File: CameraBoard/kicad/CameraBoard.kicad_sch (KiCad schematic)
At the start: 58 parts, among them IC1 MP2659GQ-0000-Z, Q1 SUD08P06-155L, Q2 SUD08P06-155L, Q3 SUD08P06-155L, U1 LM2678SD-12/NOPB

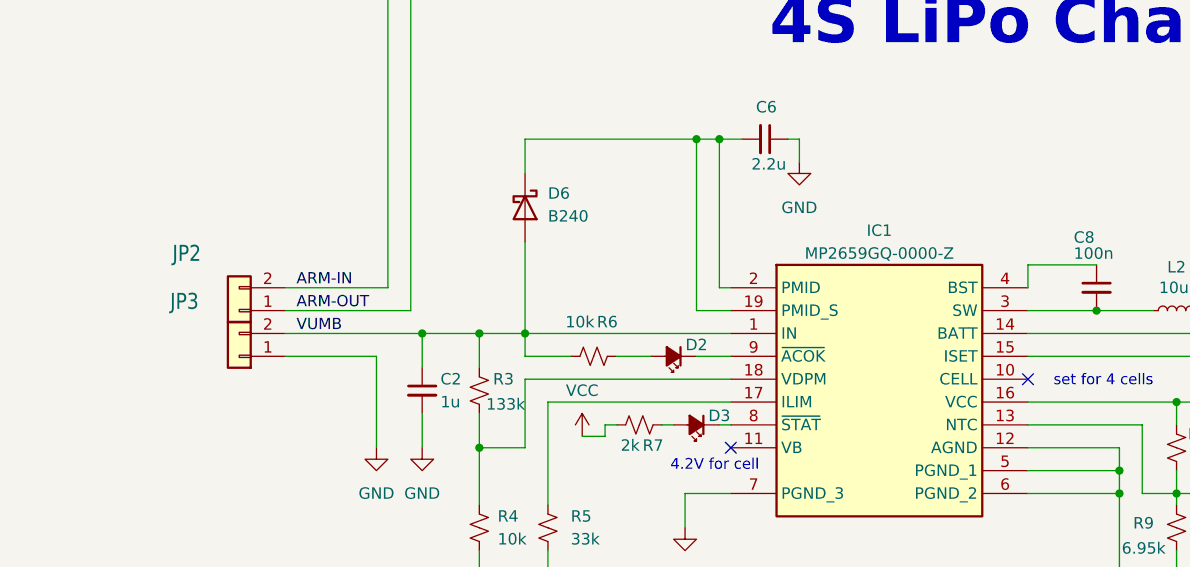
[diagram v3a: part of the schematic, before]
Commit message: PCB made from new schematic
Made the PCB. There are a few weird errors.
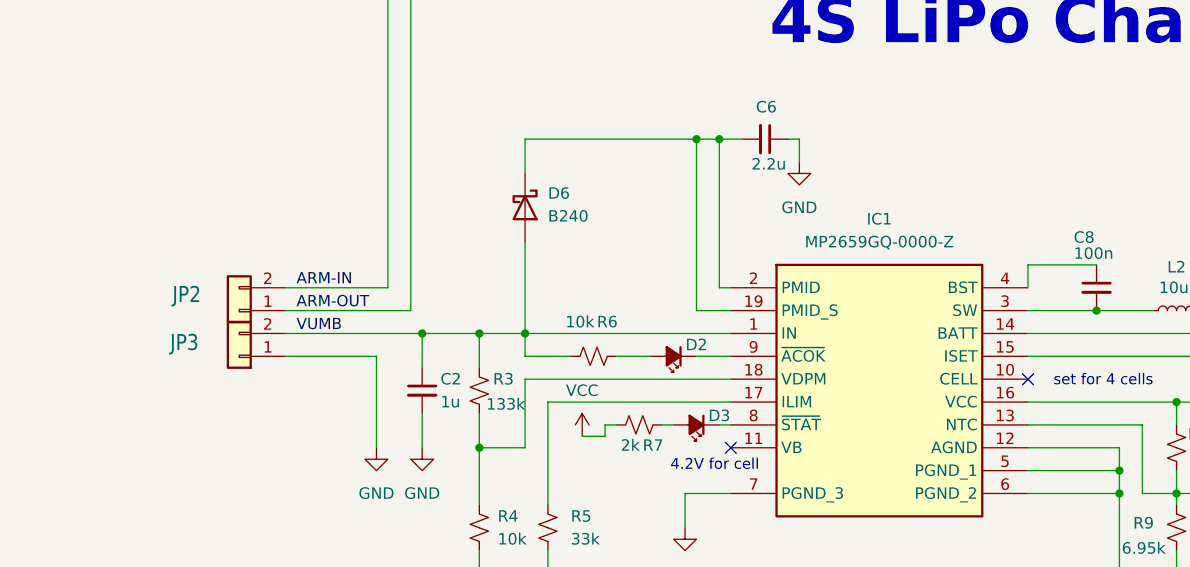
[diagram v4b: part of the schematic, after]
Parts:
- D2, D3, D5: footprint CameraBoard:CHIPLED_0603_259 -> LED_SMD:LED_0603_1608Metric
- IC1: footprint MP2659GQ0000Z -> psas-footprints:MP2659GQ0000Z; symbol MP2659GQ-0000-Z:MP2659GQ-0000-Z -> psas-libraries:MP2659GQ-0000-Z
- JP1, JP2, JP3: footprint Connector_PinHeader_2.54mm:PinHeader_1x02_P2.54mm_Vertical_SMD_Pin1Left -> Connector_PinHeader_2.54mm:PinHeader_1x02_P2.54mm_Vertical
- JP10, JP11, JP12, JP13, JP14, JP5, JP6, JP7, JP8, JP9: footprint Connector_PinHeader_2.54mm:PinHeader_1x03_P2.54mm_Vertical_SMD_Pin1Left -> Connector_PinHeader_2.54mm:PinHeader_1x03_P2.54mm_Vertical
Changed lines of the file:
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@@
 			)
 		)
-		(property "Footprint" "Connector_PinHeader_2.54mm:PinHeader_1x03_P2.54mm_Vertical_SMD_Pin1Left"
+		(property "Footprint" "Connector_PinHeader_2.54mm:PinHeader_1x03_P2.54mm_Vertical"
 			(at 271.78 238.76 0)
 			(hide yes)
@@
 			)
 		)
-		(property "Footprint" "CameraBoard:CHIPLED_0603_259"
+		(property "Footprint" "LED_SMD:LED_0603_1608Metric"
 			(at 205.74 236.22 90)
 			(hide yes)
@@
 			)
 		)
-		(property "Footprint" "Connector_PinHeader_2.54mm:PinHeader_1x03_P2.54mm_Vertical_SMD_Pin1Left"
+		(property "Footprint" "Connector_PinHeader_2.54mm:PinHeader_1x03_P2.54mm_Vertical"
 			(at 351.79 160.02 0)
 			(hide yes)
@@
 			)
 		)
-		(property "Footprint" "CameraBoard:CHIPLED_0603_259"
+		(property "Footprint" "LED_SMD:LED_0603_1608Metric"
 			(at 113.03 114.3 90)
 			(hide yes)
@@
 			)
 		)
-		(property "Footprint" "Connector_PinHeader_2.54mm:PinHeader_1x02_P2.54mm_Vertical_SMD_Pin1Left"
+		(property "Footprint" "Connector_PinHeader_2.54mm:PinHeader_1x02_P2.54mm_Vertical"
 			(at 33.02 176.53 0)
 			(hide yes)
@@
 			)
 		)
-		(property "Footprint" "Connector_PinHeader_2.54mm:PinHeader_1x03_P2.54mm_Vertical_SMD_Pin1Left"
+		(property "Footprint" "Connector_PinHeader_2.54mm:PinHeader_1x03_P2.54mm_Vertical"
 			(at 271.78 165.1 0)
 			(hide yes)
@@
 	)
 	(symbol
-		(lib_id "MP2659GQ-0000-Z:MP2659GQ-0000-Z")
-		(at 116.84 99.06 0)
+		(lib_id "psas-libraries:MP2659GQ-0000-Z")
+		(at 109.22 95.25 0)
 		(unit 1)
 		(body_style 1)
@@
 		(fields_autoplaced yes)
 		(property "Reference" "IC1"
-			(at 133.35 92.71 0)
+			(at 133.35 91.44 0)
 			(show_name no)
 			(do_not_autoplace no)
@@
 		)
 		(property "Value" "MP2659GQ-0000-Z"
-			(at 133.35 95.25 0)
+			(at 133.35 93.98 0)
 			(show_name no)
 			(do_not_autoplace no)
@@
 			)
 		)
-		(property "Footprint" "MP2659GQ0000Z"
-			(at 146.05 193.98 0)
+		(property "Footprint" "psas-footprints:MP2659GQ0000Z"
+			(at 138.43 190.17 0)
 			(hide yes)
 			(show_name no)
@@
 		)
 		(property "Datasheet" "https://www.monolithicpower.com/en/documentview/productdocument/index/version/2/document_type/Datasheet/lang/en/sku/MP2659/"
-			(at 146.05 293.98 0)
+			(at 138.43 290.17 0)
 			(hide yes)
 			(show_name no)
@@
 		)
 		(property "Description" "Battery Management 36V 3A Switching Charger with Integrated MOSFETs and Input Power Management for 3-6 Cell Batteries"
-			(at 116.84 99.06 0)
+			(at 109.22 95.25 0)
 			(hide yes)
 			(show_name no)
@@
 		)
 		(property "Height" "1"
-			(at 146.05 493.98 0)
+			(at 138.43 490.17 0)
 			(hide yes)
 			(show_name no)
@@
 		)
 		(property "Manufacturer_Name" "Monolithic Power Systems (MPS)"
-			(at 146.05 593.98 0)
+			(at 138.43 590.17 0)
 			(hide yes)
 			(show_name no)
@@
 		)
 		(property "Manufacturer_Part_Number" "MP2659GQ-0000-Z"
-			(at 146.05 693.98 0)
+			(at 138.43 690.17 0)
 			(hide yes)
 			(show_name no)
@@
 		)
 		(property "Mouser Part Number" "946-MP2659GQ-0000-Z"
-			(at 146.05 793.98 0)
+			(at 138.43 790.17 0)
 			(hide yes)
 			(show_name no)
@@
 		)
 		(property "Mouser Price/Stock" "https://www.mouser.co.uk/ProductDetail/Monolithic-Power-Systems-MPS/MP2659GQ-0000-Z?qs=yqaQSyyJnNj9lFhPiaIeCQ%3D%3D"
-			(at 146.05 893.98 0)
+			(at 138.43 890.17 0)
 			(hide yes)
 			(show_name no)
@@
 		)
 		(property "Arrow Part Number" ""
-			(at 146.05 993.98 0)
+			(at 138.43 990.17 0)
 			(hide yes)
 			(show_name no)
@@
 		)
 		(property "Arrow Price/Stock" ""
-			(at 146.05 1093.98 0)
+			(at 138.43 1090.17 0)
 			(hide yes)
 			(show_name no)
@@
 		)
 		(property "DIS" ""
-			(at 116.84 99.06 0)
+			(at 109.22 95.25 0)
 			(hide yes)
 			(show_name no)
@@
 		)
 		(property "DPN" ""
-			(at 116.84 99.06 0)
+			(at 109.22 95.25 0)
 			(hide yes)
 			(show_name no)
@@
 		)
 		(property "MAN" ""
-			(at 116.84 99.06 0)
+			(at 109.22 95.25 0)
 			(hide yes)
 			(show_name no)
@@
 		)
 		(property "MPN" ""
-			(at 116.84 99.06 0)
+			(at 109.22 95.25 0)
 			(hide yes)
 			(show_name no)
@@
 		)
 		(property "Sim.Device" ""
-			(at 116.84 99.06 0)
+			(at 109.22 95.25 0)
 			(hide yes)
 			(show_name no)
@@
 			)
 		)
-		(property "Footprint" "Connector_PinHeader_2.54mm:PinHeader_1x03_P2.54mm_Vertical_SMD_Pin1Left"
+		(property "Footprint" "Connector_PinHeader_2.54mm:PinHeader_1x03_P2.54mm_Vertical"
 			(at 271.78 177.8 0)
 			(hide yes)
@@
 			)
 		)
-		(property "Footprint" "Connector_PinHeader_2.54mm:PinHeader_1x03_P2.54mm_Vertical_SMD_Pin1Left"
+		(property "Footprint" "Connector_PinHeader_2.54mm:PinHeader_1x03_P2.54mm_Vertical"
 			(at 271.78 228.6 0)
 			(hide yes)
@@
 			)
 		)
-		(property "Footprint" "Connector_PinHeader_2.54mm:PinHeader_1x03_P2.54mm_Vertical_SMD_Pin1Left"
+		(property "Footprint" "Connector_PinHeader_2.54mm:PinHeader_1x03_P2.54mm_Vertical"
 			(at 271.78 218.44 0)
 			(hide yes)
@@
 			)
 		)
-		(property "Footprint" "Connector_PinHeader_2.54mm:PinHeader_1x03_P2.54mm_Vertical_SMD_Pin1Left"
+		(property "Footprint" "Connector_PinHeader_2.54mm:PinHeader_1x03_P2.54mm_Vertical"
 			(at 271.78 187.96 0)
 			(hide yes)
@@
 			)
 		)
-		(property "Footprint" "CameraBoard:CHIPLED_0603_259"
+		(property "Footprint" "LED_SMD:LED_0603_1608Metric"
 			(at 110.49 106.68 90)
 			(hide yes)
@@
 			)
 		)
-		(property "Footprint" "Connector_PinHeader_2.54mm:PinHeader_1x03_P2.54mm_Vertical_SMD_Pin1Left"
+		(property "Footprint" "Connector_PinHeader_2.54mm:PinHeader_1x03_P2.54mm_Vertical"
 			(at 271.78 208.28 0)
 			(hide yes)
@@
 			)
 		)
-		(property "Footprint" "Connector_PinHeader_2.54mm:PinHeader_1x03_P2.54mm_Vertical_SMD_Pin1Left"
+		(property "Footprint" "Connector_PinHeader_2.54mm:PinHeader_1x03_P2.54mm_Vertical"
 			(at 271.78 152.4 0)
 			(hide yes)
@@
 			)
 		)
-		(property "Footprint" "Connector_PinHeader_2.54mm:PinHeader_1x03_P2.54mm_Vertical_SMD_Pin1Left"
+		(property "Footprint" "Connector_PinHeader_2.54mm:PinHeader_1x03_P2.54mm_Vertical"
 			(at 271.78 198.12 0)
 			(hide yes)
@@
 		(dnp no)
 		(property "Reference" "JP2"
-			(at 56.388 95.25 0)
+			(at 56.388 99.822 0)
 			(show_name no)
 			(do_not_autoplace no)
@@
 			)
 		)
-		(property "Footprint" "Connector_PinHeader_2.54mm:PinHeader_1x02_P2.54mm_Vertical_SMD_Pin1Left"
+		(property "Footprint" "Connector_PinHeader_2.54mm:PinHeader_1x02_P2.54mm_Vertical"
 			(at 62.23 101.6 0)
 			(hide yes)
@@
 		(dnp no)
 		(property "Reference" "JP3"
-			(at 56.134 100.584 0)
+			(at 56.134 105.156 0)
 			(show_name no)
 			(do_not_autoplace no)
@@
 			)
 		)
-		(property "Footprint" "Connector_PinHeader_2.54mm:PinHeader_1x02_P2.54mm_Vertical_SMD_Pin1Left"
+		(property "Footprint" "Connector_PinHeader_2.54mm:PinHeader_1x02_P2.54mm_Vertical"
 			(at 62.23 106.68 0)
 			(hide yes)

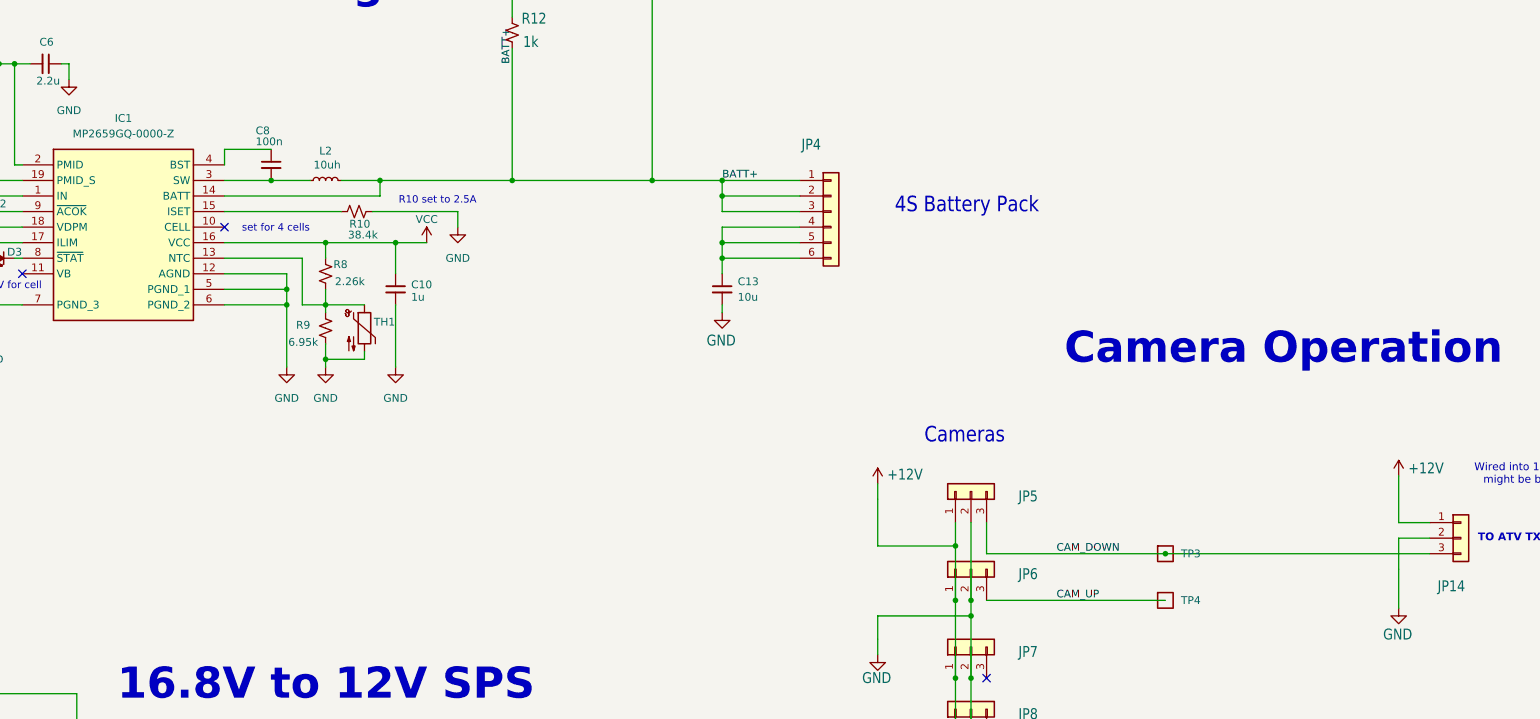
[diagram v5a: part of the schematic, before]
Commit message: Small updates to PCB
-Made text the same size
-Changed U1 symbol
-Added zones
-Moved connectors to more convenient location
-Moved leds together
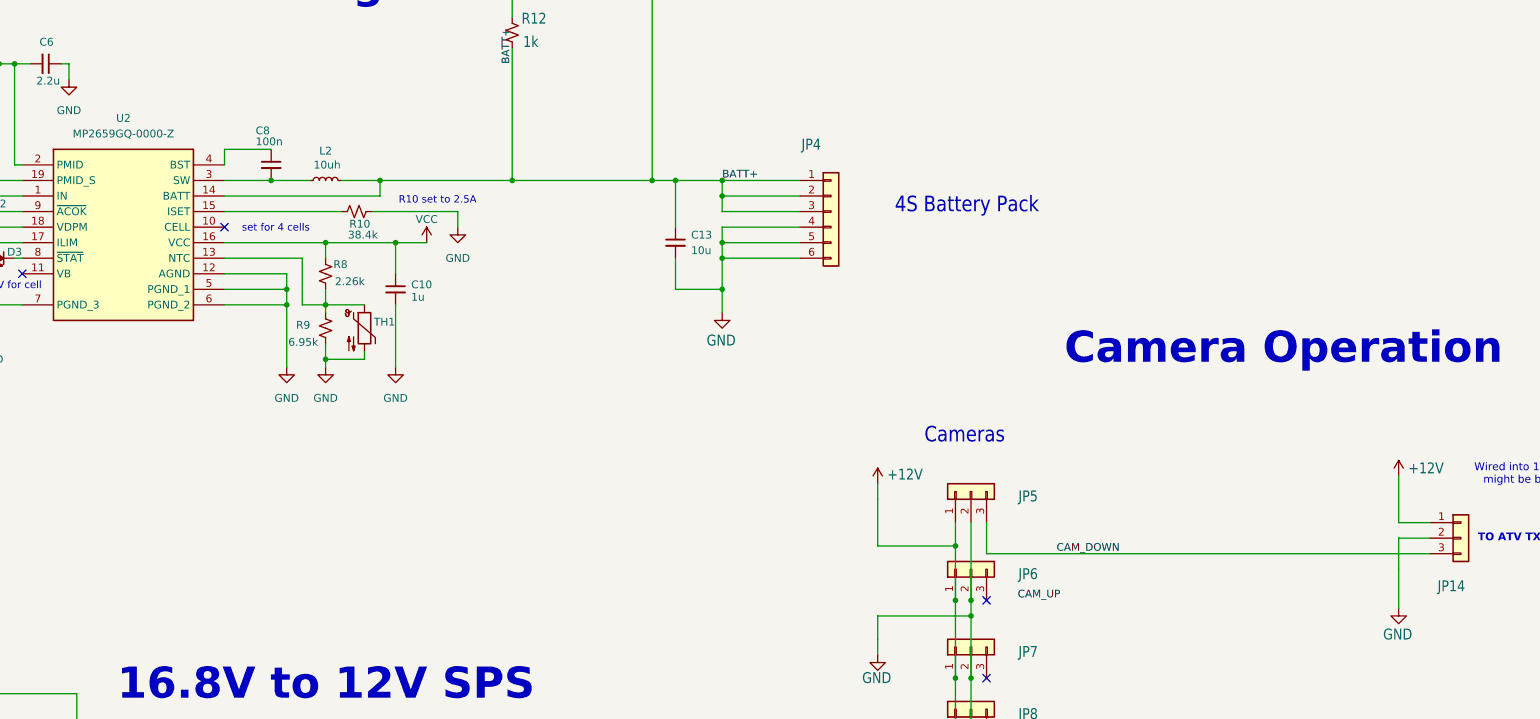
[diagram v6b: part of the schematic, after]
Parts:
- removed TP3, TP4: Test-Point, CameraBoard:2MM-TEST-POINT, symbol psas-testpoint:Test-Point
- renumbered IC1 to U2
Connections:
- net BATT+: now also C13.1
- net CAM_UP: no longer JP6.3 (Pin_3)
- net GND: now also JP4.4 (Pin_4), JP4.5 (Pin_5), JP4.6 (Pin_6)
- no-connect marks 9 -> 10
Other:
- moved on the sheet: C13
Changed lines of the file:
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@@
 	)
 	(junction
-		(at 303.53 162.56)
+		(at 231.14 114.3)
 		(diameter 0)
 		(color 0 0 0 0)
@@
 	)
 	(junction
+		(at 223.52 101.6)
+		(diameter 0)
+		(color 0 0 0 0)
+	)
+	(junction
 		(at 185.42 222.25)
 		(diameter 0)
@@
 	)
 	(junction
-		(at 87.63 185.42)
+		(at 231.14 119.38)
 		(diameter 0)
 		(color 0 0 0 0)
 	)
 	(junction
-		(at 231.14 114.3)
+		(at 87.63 185.42)
 		(diameter 0)
 		(color 0 0 0 0)
@@
 	)
 	(no_connect
+		(at 274.32 170.18)
+	)
+	(no_connect
 		(at 274.32 203.2)
 	)
@@
 	(wire
 		(pts
+			(xy 231.14 114.3) (xy 231.14 119.38)
+		)
+		(stroke
+			(width 0.1524)
+			(type solid)
+		)
+	)
+	(wire
+		(pts
 			(xy 149.86 111.76) (xy 166.37 111.76)
 		)
@@
 	(wire
 		(pts
-			(xy 231.14 121.92) (xy 231.14 123.19)
+			(xy 38.1 173.99) (xy 52.07 173.99)
 		)
 		(stroke
-			(width 0.1524)
-			(type solid)
+			(width 0)
+			(type default)
 		)
 	)
 	(wire
 		(pts
-			(xy 38.1 173.99) (xy 52.07 173.99)
+			(xy 223.52 119.38) (xy 231.14 119.38)
 		)
 		(stroke
@@
 	(wire
 		(pts
-			(xy 274.32 162.56) (xy 303.53 162.56)
-		)
-		(stroke
-			(width 0.1524)
-			(type solid)
-		)
-	)
-	(wire
-		(pts
 			(xy 153.67 222.25) (xy 158.75 222.25)
 		)
@@
 	(wire
 		(pts
-			(xy 219.71 101.6) (xy 231.14 101.6)
+			(xy 219.71 101.6) (xy 223.52 101.6)
 		)
 		(stroke
@@
 	(wire
 		(pts
-			(xy 303.53 162.56) (xy 346.71 162.56)
+			(xy 274.32 162.56) (xy 346.71 162.56)
 		)
 		(stroke
@@
 	(wire
 		(pts
-			(xy 231.14 114.3) (xy 231.14 116.84)
-		)
-		(stroke
-			(width 0.1524)
-			(type solid)
-		)
-	)
-	(wire
-		(pts
 			(xy 77.47 185.42) (xy 87.63 185.42)
 		)
@@
 	(wire
 		(pts
-			(xy 274.32 170.18) (xy 303.53 170.18)
-		)
-		(stroke
-			(width 0)
-			(type default)
-		)
-	)
-	(wire
-		(pts
 			(xy 96.52 111.76) (xy 96.52 123.19)
 		)
@@
 	(wire
 		(pts
+			(xy 223.52 114.3) (xy 223.52 119.38)
+		)
+		(stroke
+			(width 0)
+			(type default)
+		)
+	)
+	(wire
+		(pts
 			(xy 196.85 57.15) (xy 196.85 74.93)
 		)
@@
 	(wire
 		(pts
+			(xy 223.52 101.6) (xy 223.52 109.22)
+		)
+		(stroke
+			(width 0)
+			(type default)
+		)
+	)
+	(wire
+		(pts
 			(xy 269.24 161.29) (xy 269.24 170.18)
 		)
@@
 	(wire
 		(pts
+			(xy 223.52 101.6) (xy 231.14 101.6)
+		)
+		(stroke
+			(width 0)
+			(type default)
+		)
+	)
+	(wire
+		(pts
 			(xy 125.73 194.31) (xy 125.73 185.42)
 		)
@@
 	(wire
 		(pts
+			(xy 231.14 119.38) (xy 231.14 123.19)
+		)
+		(stroke
+			(width 0.1524)
+			(type solid)
+		)
+	)
+	(wire
+		(pts
 			(xy 82.55 104.14) (xy 88.9 104.14)
 		)
@@
 	)
 	(label "CAM_UP"
-		(at 285.75 170.18 0)
+		(at 279.4 170.18 0)
 		(effects
 			(font
@@
 	(symbol
 		(lib_id "Device:C_Small")
-		(at 231.14 119.38 0)
+		(at 223.52 111.76 0)
 		(unit 1)
 		(body_style 1)
@@
 		(fields_autoplaced yes)
 		(property "Reference" "C13"
-			(at 233.68 118.1162 0)
+			(at 226.06 110.4962 0)
 			(show_name no)
 			(do_not_autoplace no)
@@
 		)
 		(property "Value" "10u"
-			(at 233.68 120.6562 0)
+			(at 226.06 113.0362 0)
 			(show_name no)
 			(do_not_autoplace no)
@@
 		)
 		(property "Footprint" "Capacitor_SMD:C_1206_3216Metric"
-			(at 231.14 119.38 0)
+			(at 223.52 111.76 0)
 			(hide yes)
 			(show_name no)
@@
 		)
 		(property "Datasheet" ""
-			(at 231.14 119.38 0)
+			(at 223.52 111.76 0)
 			(hide yes)
 			(show_name no)
@@
 		)
 		(property "Description" "Unpolarized capacitor, small symbol"
-			(at 231.14 119.38 0)
+			(at 223.52 111.76 0)
 			(hide yes)
 			(show_name no)
@@
 		)
 		(property "DIS" ""
-			(at 231.14 119.38 0)
+			(at 223.52 111.76 0)
 			(hide yes)
 			(show_name no)
@@
 		)
 		(property "DPN" ""
-			(at 231.14 119.38 0)
+			(at 223.52 111.76 0)
 			(hide yes)
 			(show_name no)
@@
 		)
 		(property "MAN" ""
-			(at 231.14 119.38 0)
+			(at 223.52 111.76 0)
 			(hide yes)
 			(show_name no)
@@
 		)
 		(property "MPN" ""
-			(at 231.14 119.38 0)
+			(at 223.52 111.76 0)
 			(hide yes)
 			(show_name no)
@@
 		)
 		(property "Sim.Device" ""
-			(at 231.14 119.38 0)
+			(at 223.52 111.76 0)
 			(hide yes)
 			(show_name no)
@@
 		(dnp no)
 		(fields_autoplaced yes)
-		(property "Reference" "IC1"
+		(property "Reference" "U2"
 			(at 133.35 91.44 0)
 			(show_name no)
@@
 			(project "CameraBoard"
 				(path "/876601fa-fbd1-4e2d-9c28-84441865735b"
-					(reference "IC1")
+					(reference "U2")
 					(unit 1)
 				)
@@
 	)
 	(symbol
-		(lib_id "psas-testpoint:Test-Point")
-		(at 303.53 170.18 0)
-		(unit 1)
-		(body_style 1)
-		(exclude_from_sim no)
-		(in_bom yes)
-		(on_board yes)
-		(in_pos_files yes)
-		(dnp no)
-		(fields_autoplaced yes)
-		(property "Reference" "TP4"
-			(at 306.07 170.1799 0)
-			(show_name no)
-			(do_not_autoplace no)
-			(effects
-				(font
-					(size 1.27 1.27)
-				)
-				(justify left)
-			)
-		)
-		(property "Value" "Test-Point"
-			(at 303.53 167.64 0)
-			(hide yes)
-			(show_name no)
-			(do_not_autoplace no)
-			(effects
-				(font
-					(size 1.27 1.27)
-				)
-			)
-		)
-		(property "Footprint" "CameraBoard:2MM-TEST-POINT"
-			(at 303.53 167.64 0)
-			(hide yes)
-			(show_name no)
-			(do_not_autoplace no)
-			(effects
-				(font
-					(size 1.27 1.27)
-				)
-			)
-		)
-		(property "Datasheet" ""
-			(at 303.53 167.64 0)
-			(hide yes)
-			(show_name no)
-			(do_not_autoplace no)
-			(effects
-				(font
-					(size 1.27 1.27)
-				)
-			)
-		)
-		(property "Description" ""
-			(at 303.53 170.18 0)
-			(hide yes)
-			(show_name no)
-			(do_not_autoplace no)
-			(effects
-				(font
-					(size 1.27 1.27)
-				)
-			)
-		)
-		(pin "1"
-		)
-		(instances
-			(project "CameraBoard"
-				(path "/876601fa-fbd1-4e2d-9c28-84441865735b"
-					(reference "TP4")
-					(unit 1)
-				)
-			)
-		)
-	)
-	(symbol
 		(lib_id "Connector_Generic:Conn_01x03")
 		(at 271.78 228.6 90)
@@
 					(unit 1)
 				)
-			)
-		)
-	)
-	(symbol
-		(lib_id "psas-testpoint:Test-Point")
-		(at 303.53 162.56 0)
-		(unit 1)
-		(body_style 1)
-		(exclude_from_sim no)
-		(in_bom yes)
-		(on_board yes)
-		(in_pos_files yes)
-		(dnp no)
-		(fields_autoplaced yes)
-		(property "Reference" "TP3"
-			(at 306.07 162.5599 0)
-			(show_name no)
-			(do_not_autoplace no)
-			(effects
-				(font
-					(size 1.27 1.27)
-				)
-				(justify left)
-			)
-		)
-		(property "Value" "Test-Point"
-			(at 303.53 160.02 0)
-			(hide yes)
-			(show_name no)
-			(do_not_autoplace no)
-			(effects
-				(font
-					(size 1.27 1.27)
-				)
-			)
-		)
-		(property "Footprint" "CameraBoard:2MM-TEST-POINT"
-			(at 303.53 160.02 0)
-			(hide yes)
-			(show_name no)
-			(do_not_autoplace no)
-			(effects
-				(font
-					(size 1.27 1.27)
-				)
-			)
-		)
-		(property "Datasheet" ""
-			(at 303.53 160.02 0)
-			(hide yes)
-			(show_name no)
-			(do_not_autoplace no)
-			(effects
-				(font
-					(size 1.27 1.27)
-				)
-			)
-		)
-		(property "Description" ""
-			(at 303.53 162.56 0)
-			(hide yes)
-			(show_name no)
-			(do_not_autoplace no)
-			(effects
-				(font
-					(size 1.27 1.27)
-				)
-			)
-		)
-		(pin "1"
-		)
-		(instances
-			(project "CameraBoard"
-				(path "/876601fa-fbd1-4e2d-9c28-84441865735b"
-					(reference "TP3")
-					(unit 1)
-				)
